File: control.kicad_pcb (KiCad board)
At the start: 2 copper layers, 120 parts, among them J1 Wurth_THR_Terminal_M4, J10 TE_Faston_20-16AWG_Straight_T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, J11 TE_Faston_20-16AWG_Straight_T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, J12 TE_Faston_20-16AWG_Straight_T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, J13 TE_Faston_20-16AWG_Straight_T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, J14 TE_Faston_20-16AWG_Straight_T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, J15 TE_Faston_20-16AWG_Straight_T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, J16 TE_Faston_20-16AWG_Straight_T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, J17 TE_Faston_20-16AWG_Straight_T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, J18 TE_Faston_20-16AWG_Straight_T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, J19 TE_Faston_20-16AWG_Straight_T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, J2 Wurth_THR_Terminal_M4, J20 TE_Faston_20-16AWG_Straight_T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, J21 TE_Faston_20-16AWG_Straight_T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, J22 TE_Faston_20-16AWG_Straight_T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, J23 TE_Faston_20-16AWG_Straight_T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, J24 TE_Faston_20-16AWG_Straight_T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, J25 TE_Faston_20-16AWG_Straight_T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, J26 TE_Faston_20-16AWG_Straight_T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, J27 TE_Faston_20-16AWG_Straight_T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, J28 TE_Faston_20-16AWG_Straight_T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, J29 TE_Faston_20-16AWG_Straight_T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, J3 Wurth_THR_Terminal_M4, J30 TE_Faston_20-16AWG_Straight_T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, J31 TE_Faston_20-16AWG_Straight_T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, J32 TE_Faston_20-16AWG_Straight_T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, J4 Conn_01x03, J5 Conn_02x20_Odd_Even, J6 TE_Faston_20-16AWG_Straight_T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, J7 TE_Faston_20-16AWG_Straight_T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, J8 TE_Faston_20-16AWG_Straight_T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, J9 TE_Faston_20-16AWG_Straight_T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, Q1 ZXTN08400BFFCT, U1 TPS7B8733, U10 VND5160J, U11 VND5160J, U12 TCMT4600, U13 TCMT4600, U2 MAX33071, U3 PCA9358, U4 VND5160J, U5 VND5160J, U6 VND5160J, U7 VND5160J, U8 VND5160J, U9 VND5160J

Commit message: add compartment lights, switch to samd21j
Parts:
- removed A1: Arduino_Nano_v3.x, Module:Arduino_Nano
- removed C5, C6: 0.1uF, Capacitor_SMD:C_0805_2012Metric_Pad1.18x1.45mm_HandSolder
- removed U3: PCA9358, Package_SO:SOIC-16W_7.5x10.3mm_P1.27mm
- added C23: 0.1uF, Capacitor_SMD:C_0805_2012Metric_Pad1.18x1.45mm_HandSolder, F.Cu at (-39.7, 18.8)
- added C24: 0.1uF, Capacitor_SMD:C_0805_2012Metric_Pad1.18x1.45mm_HandSolder, F.Cu at (-39.7, 21.8)
- added C25: 6.8pF, Capacitor_SMD:C_0805_2012Metric_Pad1.18x1.45mm_HandSolder, F.Cu at (-39.7, 24.8)
- added C26: 6.8pF, Capacitor_SMD:C_0805_2012Metric_Pad1.18x1.45mm_HandSolder, F.Cu at (-39.7, 27.8)
- added C27: 10uF/16V, Capacitor_SMD:C_0805_2012Metric_Pad1.18x1.45mm_HandSolder, F.Cu at (-39.7, 30.8)
- added C28: 0.1uF, Capacitor_SMD:C_0805_2012Metric_Pad1.18x1.45mm_HandSolder, F.Cu at (-39.7, 33.8)
- added D4: LED, LED_SMD:LED_0805_2012Metric_Pad1.15x1.40mm_HandSolder, F.Cu at (-25.4, 4.46)
- added FB1: BLM18PG181SN1D, Inductor_SMD:L_0603_1608Metric_Pad1.05x0.95mm_HandSolder, F.Cu at (-25.6, 7.23)
- added J33: Conn_ARM_JTAG_SWD_10, Connector_PinHeader_1.27mm:PinHeader_2x05_P1.27mm_Vertical_SMD, F.Cu at (-27.7, 29.1)
- added R49: 39, Resistor_SMD:R_0805_2012Metric_Pad1.20x1.40mm_HandSolder, F.Cu at (-34.9, 18.8)
- added R50: 0, Resistor_SMD:R_0805_2012Metric_Pad1.20x1.40mm_HandSolder, F.Cu at (-34.9, 21.7)
- added R51: DNP, Resistor_SMD:R_0805_2012Metric_Pad1.20x1.40mm_HandSolder, F.Cu at (-34.9, 24.7)
- added R52: 91, Resistor_SMD:R_0805_2012Metric_Pad1.20x1.40mm_HandSolder, F.Cu at (-34.9, 27.6)
- added R53: 100K, Resistor_SMD:R_0805_2012Metric_Pad1.20x1.40mm_HandSolder, F.Cu at (-34.9, 30.6)
- added R54: 39, Resistor_SMD:R_0805_2012Metric_Pad1.20x1.40mm_HandSolder, F.Cu at (-34.9, 33.5)
- added SW1: SW_Push, Button_Switch_SMD:SW_Push_1P1T_NO_6x6mm_H9.5mm, F.Cu at (-27.0, 21.1)
- added U14: ATSAMD21J18A-A, Package_QFP:TQFP-64_10x10mm_P0.5mm, F.Cu at (-35.0, 10.1)
- R1: value DNP -> 120
- R2: value DNP -> 10K
- moved R6 521.8 mm to (-74.6, 13.0)
- moved R11 518.7 mm to (-74.6, 27.7), turned to 0 degrees
- moved R8 505.8 mm to (-74.6, 18.9)
- moved R7 505.7 mm to (-74.6, 15.9)
- moved R13 503.4 mm to (-69.8, 15.9)
- moved R12 502.2 mm to (-69.8, 13.0)
- moved R9 492.7 mm to (-74.6, 21.8)
- moved R10 491.8 mm to (-74.6, 24.8)
- moved R15 489.7 mm to (-69.8, 21.8)
- moved R14 489.5 mm to (-69.8, 18.9)
- moved R17 475.6 mm to (-69.8, 27.7)
- moved R20 472.2 mm to (-65.1, 18.9)
- moved R18 460.8 mm to (-65.1, 13.0)
- moved R21 460.1 mm to (-65.1, 21.8)
- moved J18 426.1 mm to (-81.5, 19.5), turned to 0 degrees
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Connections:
- net /MCU/EXT_IO0 renamed /Truck Drivers/BACKUP_EN
- net /MCU/EXT_IO1 renamed /Truck Drivers/CHIME_EN
- net /MCU/EXT_IO2 renamed /Truck Drivers/FOG_EN
- net /MCU/EXT_IO3 renamed /Truck Drivers/INTERSECT_P_EN
- net /MCU/EXT_IO4 renamed /Truck Drivers/INTERSECT_D_EN
- net /MCU/EXT_IO5 renamed /Truck Drivers/HEADLIGHT_EN
- net /MCU/EXT_IO6 renamed /Truck Drivers/MARKER_EN
- net /MCU/IO10 renamed /Signals/PARK_BRAKE_SENSE
- net /MCU/IO11 renamed /Signals/REVERSE_LIGHT_SENSE
- net /MCU/IO12 renamed /Signals/STOP_LIGHT_SENSE
- net /MCU/IO14 renamed /Signals/BATT_SW_SENSE
- net /MCU/IO4 renamed /Drivers/FLOOD_P_EN
- net /MCU/IO5 renamed /Drivers/FLOOD_R_EN
- net /MCU/IO6 renamed /Drivers/FLOOD_D_EN
- net /MCU/IO7 renamed /Signals/REAR_DOOR_SENSE
- net /MCU/IO8 renamed /Signals/SIDE_DOOR_SENSE
- net /MCU/IO9 renamed /Signals/MARKER_LIGHT_SENSE
- C21 pad 1: /MCU/IO13 -> /Signals/HORN_SENSE
- J12 pad 1: Net-(J12-Pad1) -> Net-(J12-P1-Pad1)
- J12 pad 2: Net-(J12-Pad1) -> Net-(J12-P1-Pad1)
- J13 pad 1: Net-(J13-Pad1) -> Net-(J13-P1-Pad1)
- J13 pad 2: Net-(J12-Pad1) -> Net-(J13-P1-Pad1)
- J4 pad 1: /MCU/IO13 -> /HORN_SENSE
- J4 pad 3: /MCU/EXT_IO7 -> /HORN_CTL
- R1 pad 1: /MCU/SCL -> /RS485_A
- R1 pad 2: +3.3V -> /RS485_B
- R2 pad 1: +3.3V -> /MCU/RS485_DATA_ENABLE
- R2 pad 2: /MCU/SDA -> GNDREF
- R42 pad 1: /MCU/IO13 -> /Signals/HORN_SENSE
- R43 pad 2: /MCU/IO13 -> /Signals/HORN_SENSE
- U13 pad 9: /MCU/IO13 -> /Signals/HORN_SENSE
- U2 pad 2: /MCU/IO16 -> /MCU/RS485_DATA_ENABLE
- U2 pad 3: /MCU/IO15 -> /MCU/RS485_DATA_ENABLE
- U6 pad 10: Net-(J12-Pad1) -> Net-(J12-P1-Pad1)
- U6 pad 11: Net-(J12-Pad1) -> Net-(J12-P1-Pad1)
- U6 pad 8: Net-(J12-Pad1) -> Net-(J13-P1-Pad1)
- U6 pad 9: Net-(J12-Pad1) -> Net-(J13-P1-Pad1)
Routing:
- net /MCU/IO_INT#: track 18.8 -> 0.00 mm, vias 1 -> 0
- net /MCU/IO_RST#: track 15.6 -> 0.00 mm, vias 1 -> 0
- net Net-(J12-Pad1): track 13.2 -> 0.00 mm
- net Net-(D1-A): track 11.5 -> 0.00 mm
- net /MCU/SCL: track 7.04 -> 0.00 mm
- net Net-(J8-P1-Pad1): track 6.62 -> 0.00 mm
- net Net-(J10-P1-Pad1): track 6.62 -> 0.00 mm
- net Net-(J23-P1-Pad1): track 6.62 -> 0.00 mm
- net Net-(J21-P1-Pad1): track 6.62 -> 0.00 mm
- net Net-(J18-P1-Pad1): track 6.62 -> 0.00 mm
- net Net-(J16-P1-Pad1): track 6.62 -> 0.00 mm
- net Net-(J14-P1-Pad1): track 6.62 -> 0.00 mm
- net Net-(J9-P1-Pad1): track 6.60 -> 0.00 mm
- net Net-(J11-P1-Pad1): track 6.60 -> 0.00 mm
- net Net-(J22-P1-Pad1): track 6.60 -> 0.00 mm
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
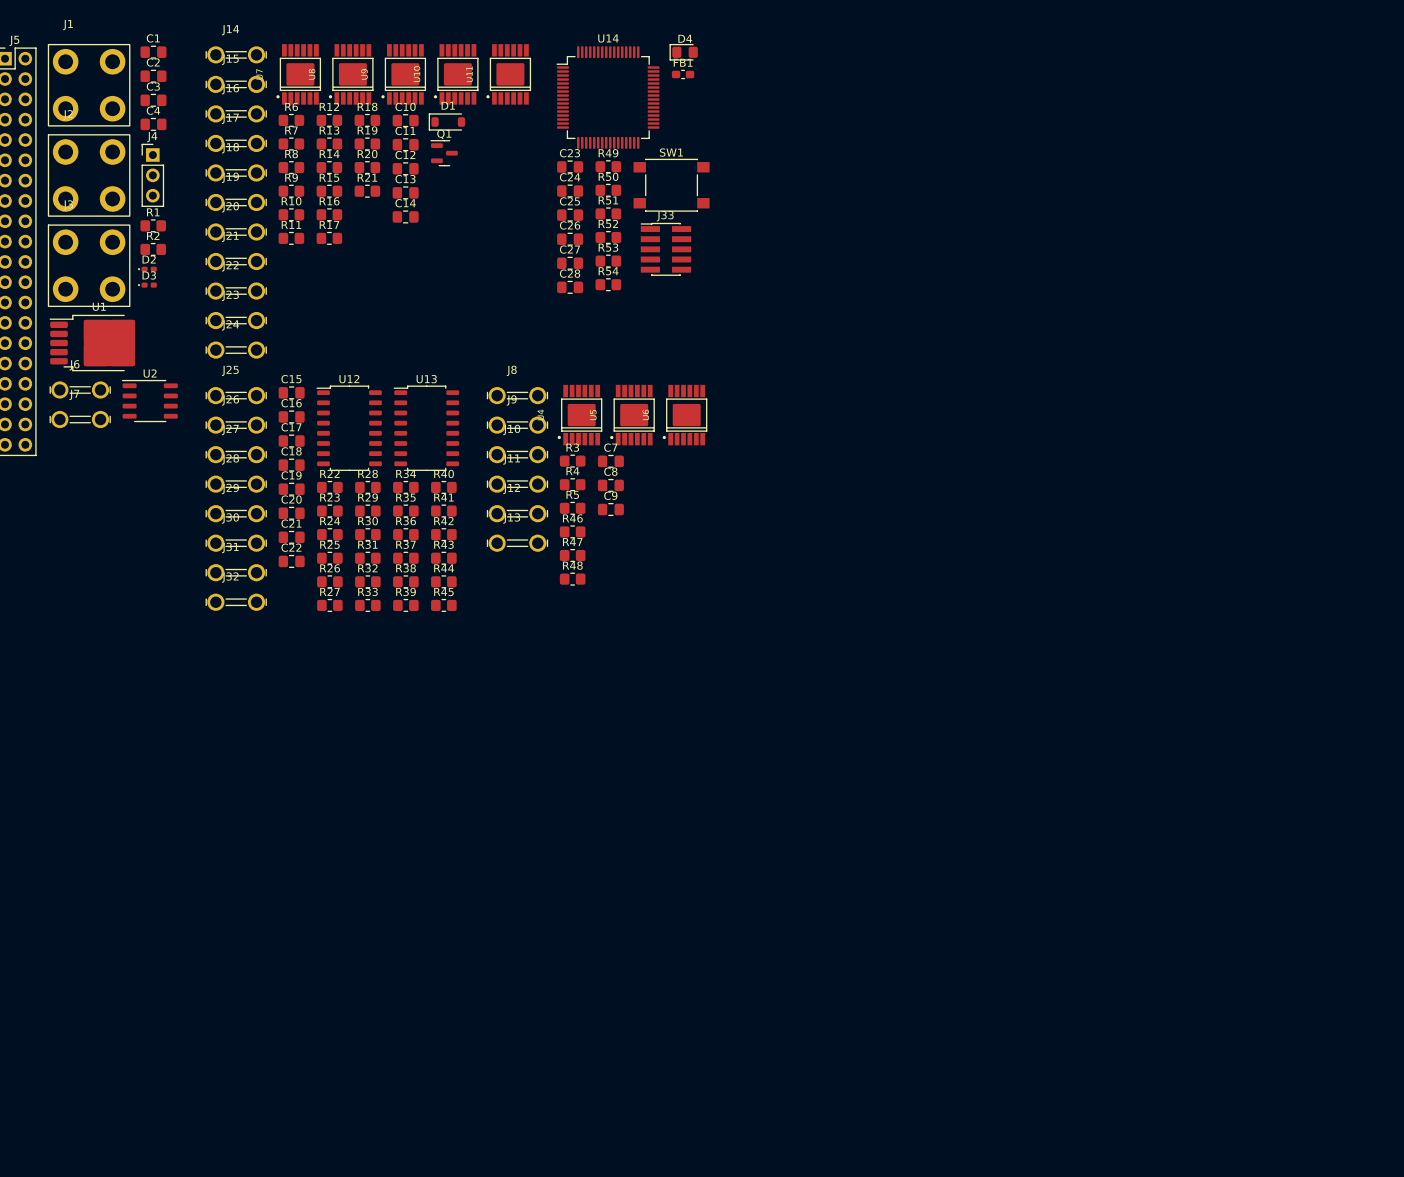
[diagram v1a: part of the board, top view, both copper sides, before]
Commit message: remove drivers
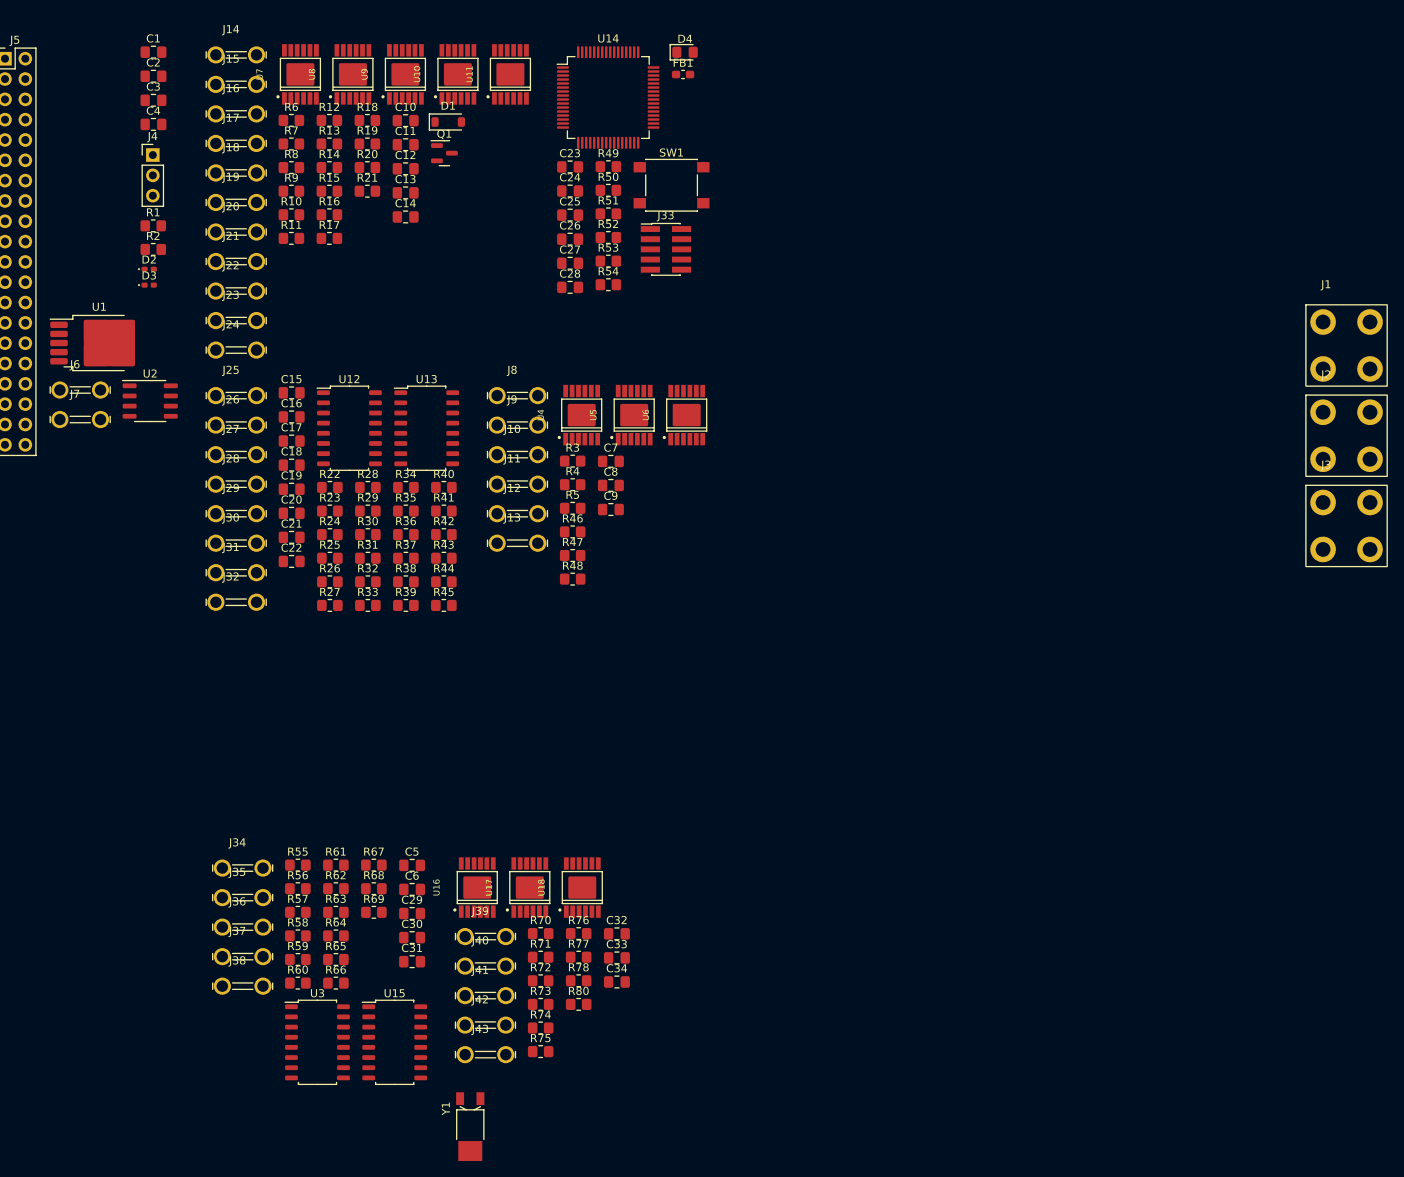
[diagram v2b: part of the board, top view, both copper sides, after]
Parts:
- added C29: 1uF, Capacitor_SMD:C_0805_2012Metric_Pad1.18x1.45mm_HandSolder, F.Cu at (-59.5, 112.1)
- added C30: 1uF, Capacitor_SMD:C_0805_2012Metric_Pad1.18x1.45mm_HandSolder, F.Cu at (-59.5, 115.1)
- added C31: 1uF, Capacitor_SMD:C_0805_2012Metric_Pad1.18x1.45mm_HandSolder, F.Cu at (-59.5, 118.1)
- added C32: DNP, Capacitor_SMD:C_0805_2012Metric_Pad1.18x1.45mm_HandSolder, F.Cu at (-33.9, 114.7)
- added C33: DNP, Capacitor_SMD:C_0805_2012Metric_Pad1.18x1.45mm_HandSolder, F.Cu at (-33.9, 117.7)
- added C34: DNP, Capacitor_SMD:C_0805_2012Metric_Pad1.18x1.45mm_HandSolder, F.Cu at (-33.9, 120.7)
- added C5: 1uF, Capacitor_SMD:C_0805_2012Metric_Pad1.18x1.45mm_HandSolder, F.Cu at (-59.5, 106.1)
- added C6: 1uF, Capacitor_SMD:C_0805_2012Metric_Pad1.18x1.45mm_HandSolder, F.Cu at (-59.5, 109.1)
- added J34: TE_Faston_20-16AWG_Straight_Tab, Toadly:TE_Faston_20-16AWG_Straight_Tab, F.Cu at (-80.7, 106.4)
- added J35: TE_Faston_20-16AWG_Straight_Tab, Toadly:TE_Faston_20-16AWG_Straight_Tab, F.Cu at (-80.7, 110.1)
- added J36: TE_Faston_20-16AWG_Straight_Tab, Toadly:TE_Faston_20-16AWG_Straight_Tab, F.Cu at (-80.7, 113.8)
- added J37: TE_Faston_20-16AWG_Straight_Tab, Toadly:TE_Faston_20-16AWG_Straight_Tab, F.Cu at (-80.7, 117.5)
- added J38: TE_Faston_20-16AWG_Straight_Tab, Toadly:TE_Faston_20-16AWG_Straight_Tab, F.Cu at (-80.7, 121.2)
- added J39: TE_Faston_20-16AWG_Straight_Tab, Toadly:TE_Faston_20-16AWG_Straight_Tab, F.Cu at (-50.3, 115.0)
- added J40: TE_Faston_20-16AWG_Straight_Tab, Toadly:TE_Faston_20-16AWG_Straight_Tab, F.Cu at (-50.3, 118.7)
- added J41: TE_Faston_20-16AWG_Straight_Tab, Toadly:TE_Faston_20-16AWG_Straight_Tab, F.Cu at (-50.3, 122.4)
- added J42: TE_Faston_20-16AWG_Straight_Tab, Toadly:TE_Faston_20-16AWG_Straight_Tab, F.Cu at (-50.3, 126.1)
- added J43: TE_Faston_20-16AWG_Straight_Tab, Toadly:TE_Faston_20-16AWG_Straight_Tab, F.Cu at (-50.3, 129.8)
- added R55: 3.3k, Resistor_SMD:R_0805_2012Metric_Pad1.20x1.40mm_HandSolder, F.Cu at (-73.8, 106.1)
- added R56: 3.3k, Resistor_SMD:R_0805_2012Metric_Pad1.20x1.40mm_HandSolder, F.Cu at (-73.8, 109.0)
- added R57: 3.3k, Resistor_SMD:R_0805_2012Metric_Pad1.20x1.40mm_HandSolder, F.Cu at (-73.8, 112.0)
- added R58: 3.3k, Resistor_SMD:R_0805_2012Metric_Pad1.20x1.40mm_HandSolder, F.Cu at (-73.8, 114.9)
- added R59: DNP, Resistor_SMD:R_0805_2012Metric_Pad1.20x1.40mm_HandSolder, F.Cu at (-73.8, 117.9)
- added R60: 1.1k, Resistor_SMD:R_0805_2012Metric_Pad1.20x1.40mm_HandSolder, F.Cu at (-73.8, 120.8)
- added R61: DNP, Resistor_SMD:R_0805_2012Metric_Pad1.20x1.40mm_HandSolder, F.Cu at (-69.0, 106.1)
- added R62: 1.1k, Resistor_SMD:R_0805_2012Metric_Pad1.20x1.40mm_HandSolder, F.Cu at (-69.0, 109.0)
- added R63: DNP, Resistor_SMD:R_0805_2012Metric_Pad1.20x1.40mm_HandSolder, F.Cu at (-69.0, 112.0)
- added R64: 1.1k, Resistor_SMD:R_0805_2012Metric_Pad1.20x1.40mm_HandSolder, F.Cu at (-69.0, 114.9)
- added R65: DNP, Resistor_SMD:R_0805_2012Metric_Pad1.20x1.40mm_HandSolder, F.Cu at (-69.0, 117.9)
- added R66: 1.1k, Resistor_SMD:R_0805_2012Metric_Pad1.20x1.40mm_HandSolder, F.Cu at (-69.0, 120.8)
- added R67: 3.3k, Resistor_SMD:R_0805_2012Metric_Pad1.20x1.40mm_HandSolder, F.Cu at (-64.2, 106.1)
- added R68: DNP, Resistor_SMD:R_0805_2012Metric_Pad1.20x1.40mm_HandSolder, F.Cu at (-64.2, 109.0)
- added R69: 1.1k, Resistor_SMD:R_0805_2012Metric_Pad1.20x1.40mm_HandSolder, F.Cu at (-64.2, 112.0)
- added R70: 10k, Resistor_SMD:R_0805_2012Metric_Pad1.20x1.40mm_HandSolder, F.Cu at (-43.4, 114.6)
- added R71: 10k, Resistor_SMD:R_0805_2012Metric_Pad1.20x1.40mm_HandSolder, F.Cu at (-43.4, 117.6)
- added R72: 10k, Resistor_SMD:R_0805_2012Metric_Pad1.20x1.40mm_HandSolder, F.Cu at (-43.4, 120.5)
- added R73: 10k, Resistor_SMD:R_0805_2012Metric_Pad1.20x1.40mm_HandSolder, F.Cu at (-43.4, 123.5)
- added R74: 10k, Resistor_SMD:R_0805_2012Metric_Pad1.20x1.40mm_HandSolder, F.Cu at (-43.4, 126.4)
- added R75: 10k, Resistor_SMD:R_0805_2012Metric_Pad1.20x1.40mm_HandSolder, F.Cu at (-43.4, 129.4)
- added R76: 10k, Resistor_SMD:R_0805_2012Metric_Pad1.20x1.40mm_HandSolder, F.Cu at (-38.6, 114.6)
- added R77: 10k, Resistor_SMD:R_0805_2012Metric_Pad1.20x1.40mm_HandSolder, F.Cu at (-38.6, 117.6)
- added R78: 10k, Resistor_SMD:R_0805_2012Metric_Pad1.20x1.40mm_HandSolder, F.Cu at (-38.6, 120.5)
- added R80: 10k, Resistor_SMD:R_0805_2012Metric_Pad1.20x1.40mm_HandSolder, F.Cu at (-38.6, 123.5)
- added U15: TCMT4600, Package_SO:SOP-16_4.55x10.3mm_P1.27mm, F.Cu at (-61.6, 128.2)
- added U16: VND5160J, Toadly:POWERSSO-12, F.Cu at (-51.3, 108.9)
- added U17: VND5160J, Toadly:POWERSSO-12, F.Cu at (-44.8, 108.9)
- added U18: VND5160J, Toadly:POWERSSO-12, F.Cu at (-38.2, 108.9)
- added U3: TCMT4600, Package_SO:SOP-16_4.55x10.3mm_P1.27mm, F.Cu at (-71.3, 128.2)
- added Y1: Crystal, Crystal:Crystal_SMD_MicroCrystal_MS1V-T1K, F.Cu at (-52.2, 138.8)
- moved J1 160.5 mm to (57.3, 41.1)
- moved J2 160.5 mm to (57.3, 52.4)
- moved J3 160.5 mm to (57.3, 63.7)
